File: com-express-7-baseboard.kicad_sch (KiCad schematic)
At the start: 0 parts

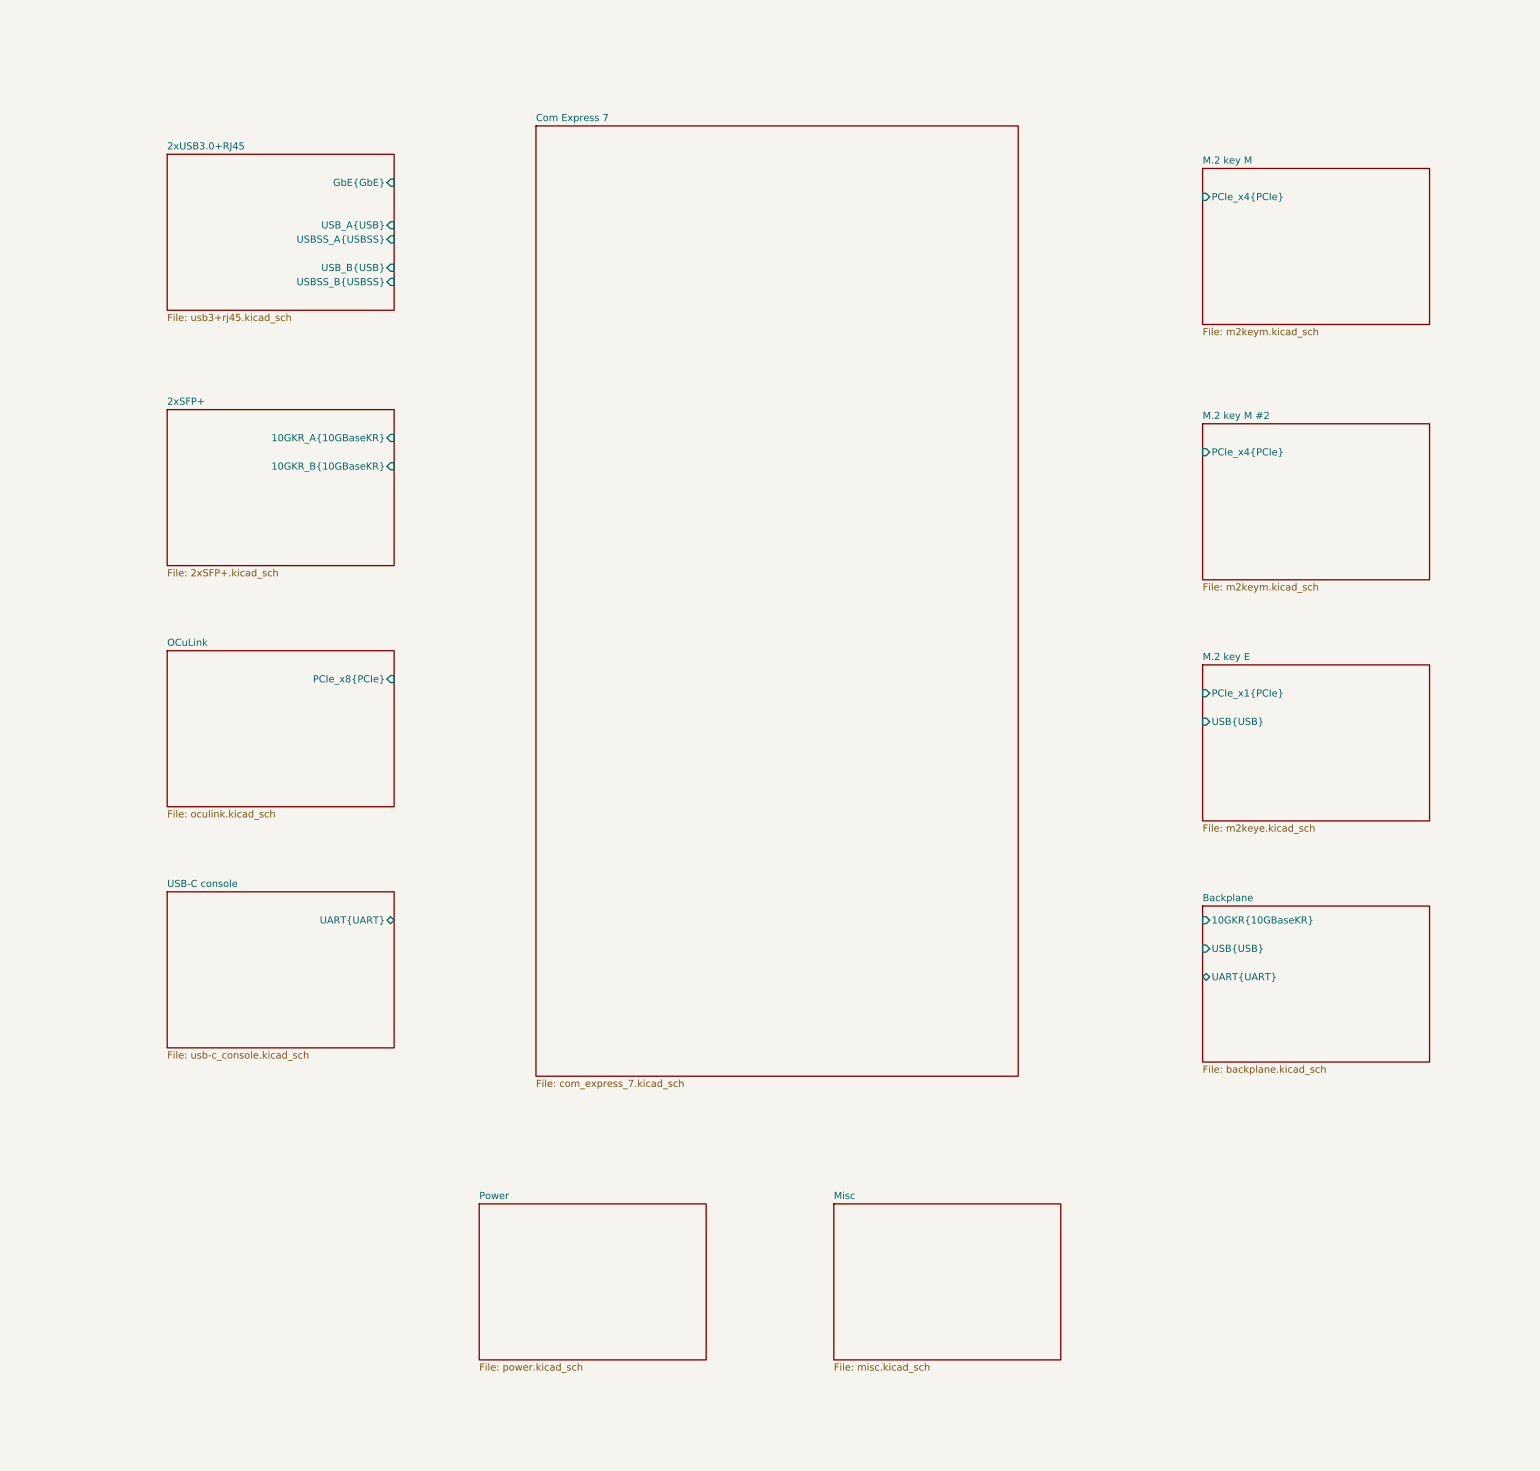
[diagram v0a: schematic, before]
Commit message: [#56643] Create buses for interfaces, assign buses to blocks
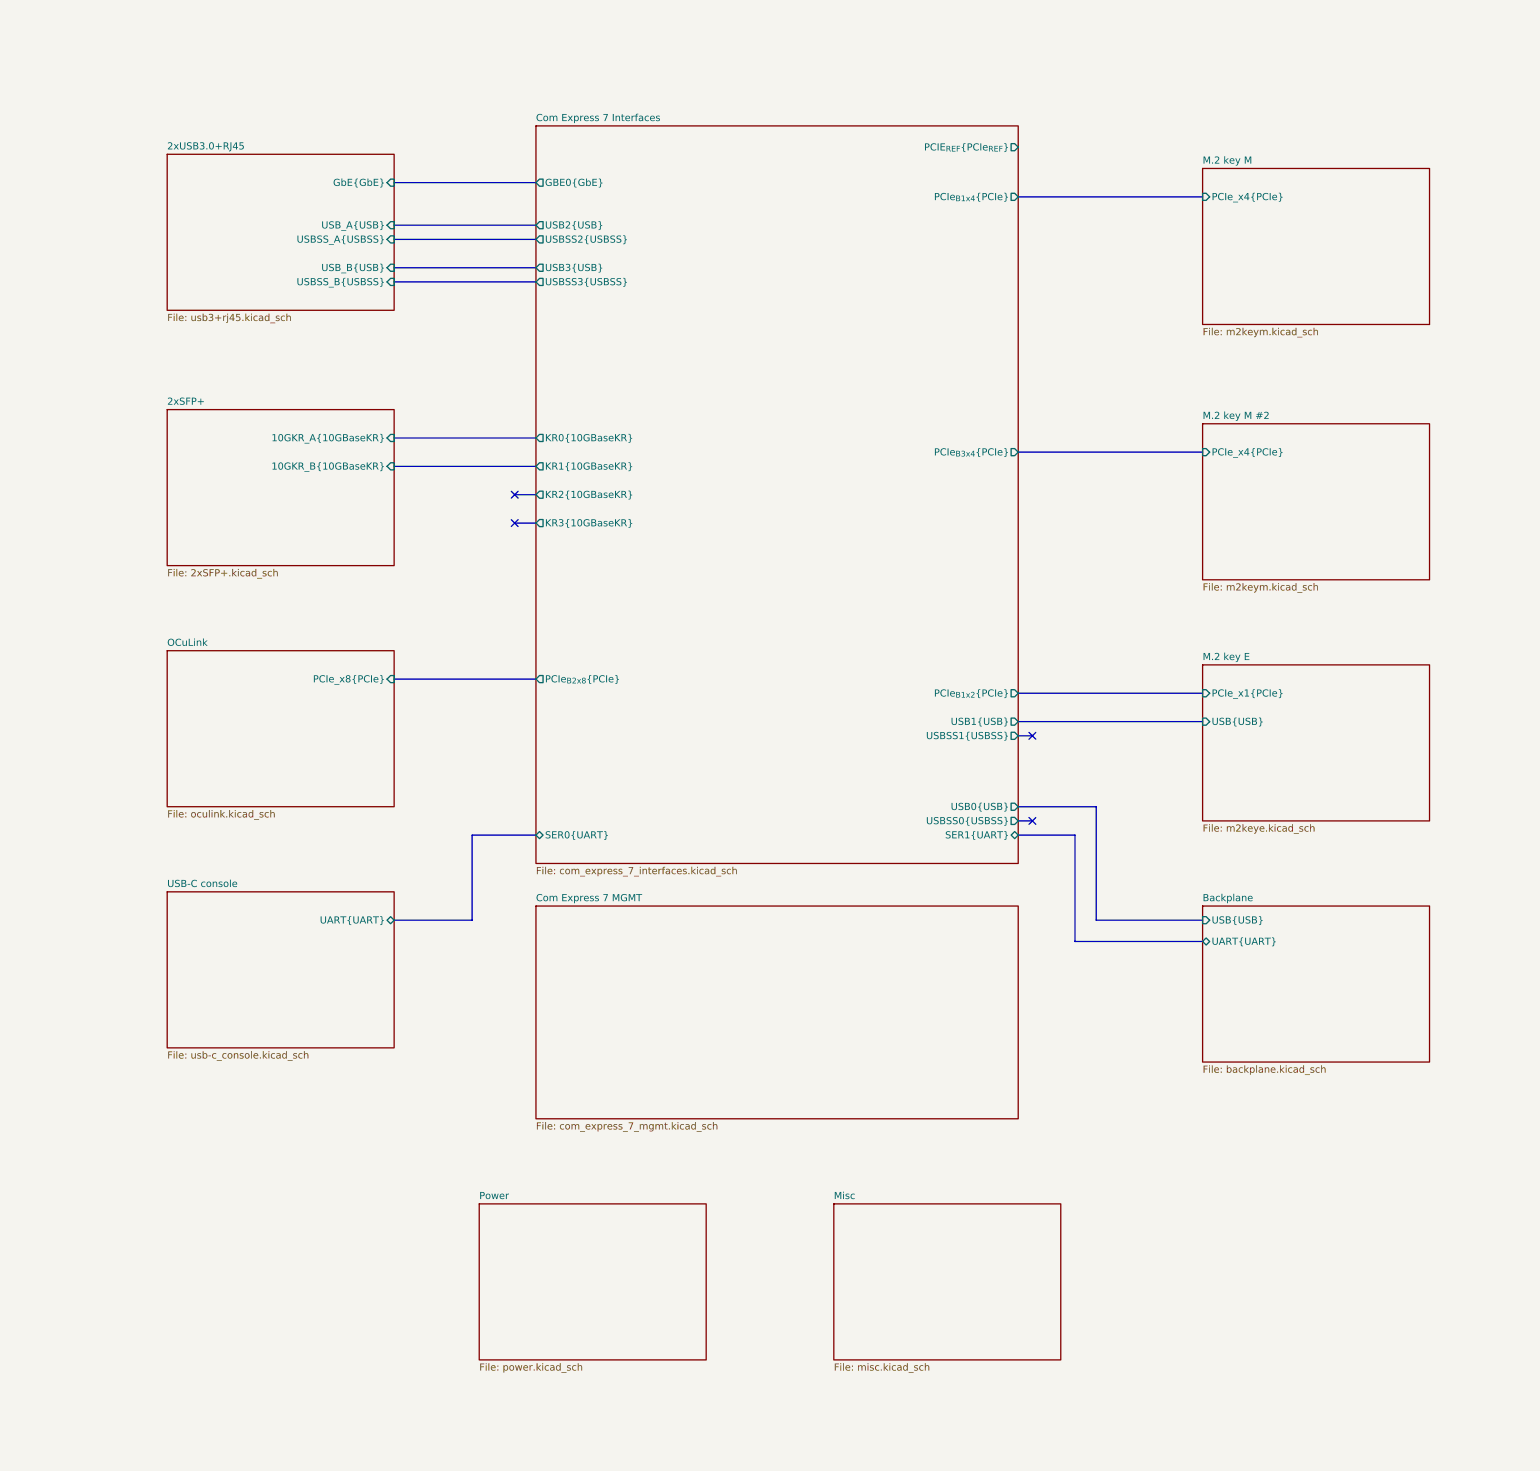
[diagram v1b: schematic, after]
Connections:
- no-connect marks 0 -> 4
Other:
- sheet Com Express 7 renamed Com Express 7 Interfaces
- added sheet Com Express 7 MGMT (com_express_7_mgmt.kicad_sch)
- sheet Backplane ports: added none; removed 10GKR{10GBaseKR}
- sheet Com Express 7 Interfaces: file com_express_7.kicad_sch -> com_express_7_interfaces.kicad_sch
- sheet Com Express 7 Interfaces ports: added GBE0{GbE}, KR0{10GBaseKR}, KR1{10GBaseKR}, KR2{10GBaseKR}, KR3{10GBaseKR}, PCIE_{REF}{PCIe_{REF}}, PCIe_{B1x2}{PCIe}, PCIe_{B1x4}{PCIe}, PCIe_{B2x8}{PCIe}, PCIe_{B3x4}{PCIe}, SER0{UART}, SER1{UART}, USB0{USB}, USB1{USB}, USB2{USB}, USB3{USB}, USBSS0{USBSS}, USBSS1{USBSS}, USBSS2{USBSS}, USBSS3{USBSS}; removed none
- company: (none) -> Antmicro Ltd.
- title: (none) -> Com Express 7 baseboard
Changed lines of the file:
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@@
 (kicad_sch (version 20230121) (generator eeschema)
   (paper "A3")
-  (bus_alias "10GBaseKR" (members ))
-  (bus_alias "GbE" (members ))
-  (bus_alias "PCIe" (members ))
-  (bus_alias "USB" (members ))
-  (bus_alias "USBSS" (members ))
+  (title_block
+    (title "Com Express 7 baseboard")
+    (date "2024-03-22")
+    (rev "1.0.0")
+    (company "Antmicro Ltd.")
+  )
+  (bus_alias "10GBaseKR" (members "TX+" "TX-" "RX+" "RX-"))
+  (bus_alias "GbE" (members "MDI3+" "MDI3-" "MDI2+" "MDI2-" "MDI1+" "MDI1-" "MDI0+" "MDI0-" "CTREF"))
+  (bus_alias "PCIe" (members "TX7+" "TX7-" "TX6+" "TX6-" "TX5+" "TX5-" "TX4+" "TX4-" "TX3+" "TX3-" "TX2+" "TX2-" "TX1+" "TX1-" "TX0+" "TX0-" "RX7+" "RX7-" "RX6+" "RX6-" "RX5+" "RX5-" "RX4+" "RX4-" "RX3+" "RX3-" "RX2+" "RX2-" "RX1+" "RX1-" "RX0+" "RX0-"))
+  (bus_alias "USB" (members "D+" "D-"))
+  (bus_alias "USBSS" (members "TX+" "TX-" "RX+" "RX-"))
+  (no_connect (at 251.46 147.32))
+  (no_connect (at 158.75 109.22))
+  (no_connect (at 158.75 104.14))
+  (no_connect (at 251.46 162.56))
+  (bus (pts (xy 259.08 184.15) (xy 281.94 184.15))
+    (stroke (width 0) (type default) (color 255 153 0 1))
+  )
+  (bus (pts (xy 248.92 144.78) (xy 281.94 144.78))
+    (stroke (width 0) (type default) (color 0 0 255 1))
+  )
+  (bus (pts (xy 137.16 58.42) (xy 162.56 58.42))
+    (stroke (width 0) (type default) (color 0 255 255 1))
+  )
+  (bus (pts (xy 137.16 48.26) (xy 162.56 48.26))
+    (stroke (width 0) (type default))
+  )
+  (bus (pts (xy 137.16 99.06) (xy 162.56 99.06))
+    (stroke (width 0) (type default) (color 255 0 0 1))
+  )
+  (bus (pts (xy 262.89 180.34) (xy 281.94 180.34))
+    (stroke (width 0) (type default) (color 0 0 255 1))
+  )
+  (bus (pts (xy 137.16 55.88) (xy 162.56 55.88))
+    (stroke (width 0) (type default) (color 0 0 255 1))
+  )
+  (bus (pts (xy 248.92 147.32) (xy 251.46 147.32))
+    (stroke (width 0) (type default))
+  )
+  (bus (pts (xy 248.92 162.56) (xy 251.46 162.56))
+    (stroke (width 0) (type default) (color 0 255 255 1))
+  )
+  (bus (pts (xy 162.56 165.1) (xy 151.13 165.1))
+    (stroke (width 0) (type default) (color 255 153 0 1))
+  )
+  (bus (pts (xy 259.08 165.1) (xy 259.08 184.15))
+    (stroke (width 0) (type default) (color 255 153 0 1))
+  )
+  (bus (pts (xy 158.75 104.14) (xy 162.56 104.14))
+    (stroke (width 0) (type default) (color 255 0 0 1))
+  )
+  (bus (pts (xy 137.16 63.5) (xy 162.56 63.5))
+    (stroke (width 0) (type default) (color 0 0 255 1))
+  )
+  (bus (pts (xy 137.16 66.04) (xy 162.56 66.04))
+    (stroke (width 0) (type default) (color 0 255 255 1))
+  )
+  (bus (pts (xy 248.92 96.52) (xy 281.94 96.52))
+    (stroke (width 0) (type default) (color 194 0 194 1))
+  )
+  (bus (pts (xy 151.13 165.1) (xy 151.13 180.34))
+    (stroke (width 0) (type default) (color 255 153 0 1))
+  )
+  (bus (pts (xy 137.16 137.16) (xy 162.56 137.16))
+    (stroke (width 0) (type default) (color 194 0 194 1))
+  )
+  (bus (pts (xy 151.13 180.34) (xy 137.16 180.34))
+    (stroke (width 0) (type default) (color 255 153 0 1))
+  )
+  (bus (pts (xy 248.92 160.02) (xy 262.89 160.02))
+    (stroke (width 0) (type default) (color 0 0 255 1))
+  )
+  (bus (pts (xy 248.92 165.1) (xy 259.08 165.1))
+    (stroke (width 0) (type default) (color 255 153 0 1))
+  )
+  (bus (pts (xy 248.92 50.8) (xy 281.94 50.8))
+    (stroke (width 0) (type default) (color 194 0 194 1))
+  )
+  (bus (pts (xy 158.75 109.22) (xy 162.56 109.22))
+    (stroke (width 0) (type default) (color 255 0 0 1))
+  )
+  (bus (pts (xy 248.92 139.7) (xy 281.94 139.7))
+    (stroke (width 0) (type default) (color 194 0 194 1))
+  )
+  (bus (pts (xy 137.16 93.98) (xy 162.56 93.98))
+    (stroke (width 0) (type default) (color 255 0 0 1))
+  )
+  (bus (pts (xy 262.89 160.02) (xy 262.89 180.34))
+    (stroke (width 0) (type default) (color 0 0 255 1))
+  )
   (sheet (at 281.94 45.72) (size 40.64 27.94) (fields_autoplaced)
     (stroke (width 0.1524) (type solid))
@@
       (effects (font (size 1.27 1.27)) (justify left top))
     )
-    (pin "USB{USB}" input (at 281.94 185.42 180)
-      (effects (font (size 1.27 1.27)) (justify left))
-    )
-    (pin "10GKR{10GBaseKR}" input (at 281.94 180.34 180)
-      (effects (font (size 1.27 1.27)) (justify left))
-    )
-    (pin "UART{UART}" bidirectional (at 281.94 190.5 180)
+    (pin "USB{USB}" input (at 281.94 180.34 180)
+      (effects (font (size 1.27 1.27)) (justify left))
+    )
+    (pin "UART{UART}" bidirectional (at 281.94 184.15 180)
       (effects (font (size 1.27 1.27)) (justify left))
     )
@@
     )
   )
-  (sheet (at 162.56 38.1) (size 86.36 170.18) (fields_autoplaced)
-    (stroke (width 0.1524) (type solid))
-    (fill (color 0 0 0 0.0000))
-    (property "Sheetname" "Com Express 7" (at 162.56 37.3884 0)
-      (effects (font (size 1.27 1.27)) (justify left bottom))
-    )
-    (property "Sheetfile" "com_express_7.kicad_sch" (at 162.56 208.8646 0)
-      (effects (font (size 1.27 1.27)) (justify left top))
+  (sheet (at 162.56 38.1) (size 86.36 132.08) (fields_autoplaced)
+    (stroke (width 0.1524) (type solid))
+    (fill (color 0 0 0 0.0000))
+    (property "Sheetname" "Com Express 7 Interfaces" (at 162.56 37.3884 0)
+      (effects (font (size 1.27 1.27)) (justify left bottom))
+    )
+    (property "Sheetfile" "com_express_7_interfaces.kicad_sch" (at 162.56 170.7646 0)
+      (effects (font (size 1.27 1.27)) (justify left top))
+    )
+    (pin "PCIe_{B2x8}{PCIe}" output (at 162.56 137.16 180)
+      (effects (font (size 1.27 1.27)) (justify left))
+    )
+    (pin "PCIe_{B1x4}{PCIe}" output (at 248.92 50.8 0)
+      (effects (font (size 1.27 1.27)) (justify right))
+    )
+    (pin "PCIe_{B1x2}{PCIe}" output (at 248.92 139.7 0)
+      (effects (font (size 1.27 1.27)) (justify right))
+    )
+    (pin "USB0{USB}" output (at 248.92 160.02 0)
+      (effects (font (size 1.27 1.27)) (justify right))
+    )
+    (pin "KR0{10GBaseKR}" output (at 162.56 93.98 180)
+      (effects (font (size 1.27 1.27)) (justify left))
+    )
+    (pin "KR1{10GBaseKR}" output (at 162.56 99.06 180)
+      (effects (font (size 1.27 1.27)) (justify left))
+    )
+    (pin "KR3{10GBaseKR}" output (at 162.56 109.22 180)
+      (effects (font (size 1.27 1.27)) (justify left))
+    )
+    (pin "KR2{10GBaseKR}" output (at 162.56 104.14 180)
+      (effects (font (size 1.27 1.27)) (justify left))
+    )
+    (pin "PCIe_{B3x4}{PCIe}" output (at 248.92 96.52 0)
+      (effects (font (size 1.27 1.27)) (justify right))
+    )
+    (pin "GBE0{GbE}" output (at 162.56 48.26 180)
+      (effects (font (size 1.27 1.27)) (justify left))
+    )
+    (pin "PCIE_{REF}{PCIe_{REF}}" output (at 248.92 41.91 0)
+      (effects (font (size 1.27 1.27)) (justify right))
+    )
+    (pin "USB3{USB}" output (at 162.56 63.5 180)
+      (effects (font (size 1.27 1.27)) (justify left))
+    )
+    (pin "USB2{USB}" output (at 162.56 55.88 180)
+      (effects (font (size 1.27 1.27)) (justify left))
+    )
+    (pin "USB1{USB}" output (at 248.92 144.78 0)
+      (effects (font (size 1.27 1.27)) (justify right))
+    )
+    (pin "USBSS3{USBSS}" output (at 162.56 66.04 180)
+      (effects (font (size 1.27 1.27)) (justify left))
+    )
+    (pin "USBSS2{USBSS}" output (at 162.56 58.42 180)
+      (effects (font (size 1.27 1.27)) (justify left))
+    )
+    (pin "USBSS1{USBSS}" output (at 248.92 147.32 0)
+      (effects (font (size 1.27 1.27)) (justify right))
+    )
+    (pin "USBSS0{USBSS}" output (at 248.92 162.56 0)
+      (effects (font (size 1.27 1.27)) (justify right))
+    )
+    (pin "SER0{UART}" bidirectional (at 162.56 165.1 180)
+      (effects (font (size 1.27 1.27)) (justify left))
+    )
+    (pin "SER1{UART}" bidirectional (at 248.92 165.1 0)
+      (effects (font (size 1.27 1.27)) (justify right))
     )
     (instances
@@
       )
     )
+  )
+  (sheet (at 162.56 177.8) (size 86.36 38.1) (fields_autoplaced)
+    (stroke (width 0.1524) (type solid))
+    (fill (color 0 0 0 0.0000))
+    (property "Sheetname" "Com Express 7 MGMT" (at 162.56 177.0884 0)
+      (effects (font (size 1.27 1.27)) (justify left bottom))
+    )
+    (property "Sheetfile" "com_express_7_mgmt.kicad_sch" (at 162.56 216.4846 0)
+      (effects (font (size 1.27 1.27)) (justify left top))
+    )
+    (instances
+      (project "com-express-7-baseboard"
+        (path "/1b8c34da-dad5-4b0b-8c4b-45db766c4dfa" (page "13"))
+      )
+    )
